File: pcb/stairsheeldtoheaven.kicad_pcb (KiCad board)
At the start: 2 copper layers, 105.4 x 97.8 mm, 27 parts, among them P1 CONN_10X2, P10 5, P11 6, P12 7, P13 8, P14 9, P15 10, P16 11, P17 12, P18 13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

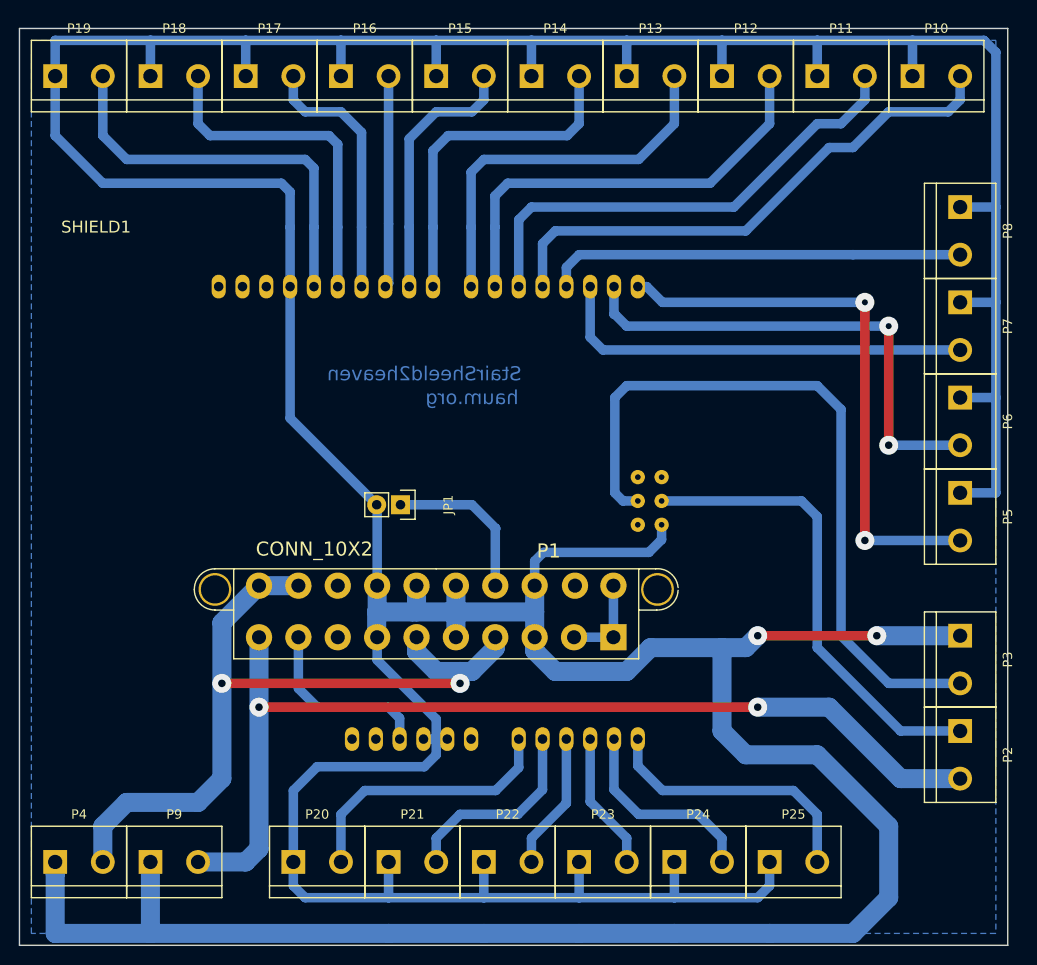
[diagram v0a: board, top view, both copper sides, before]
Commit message: simplification connection LED
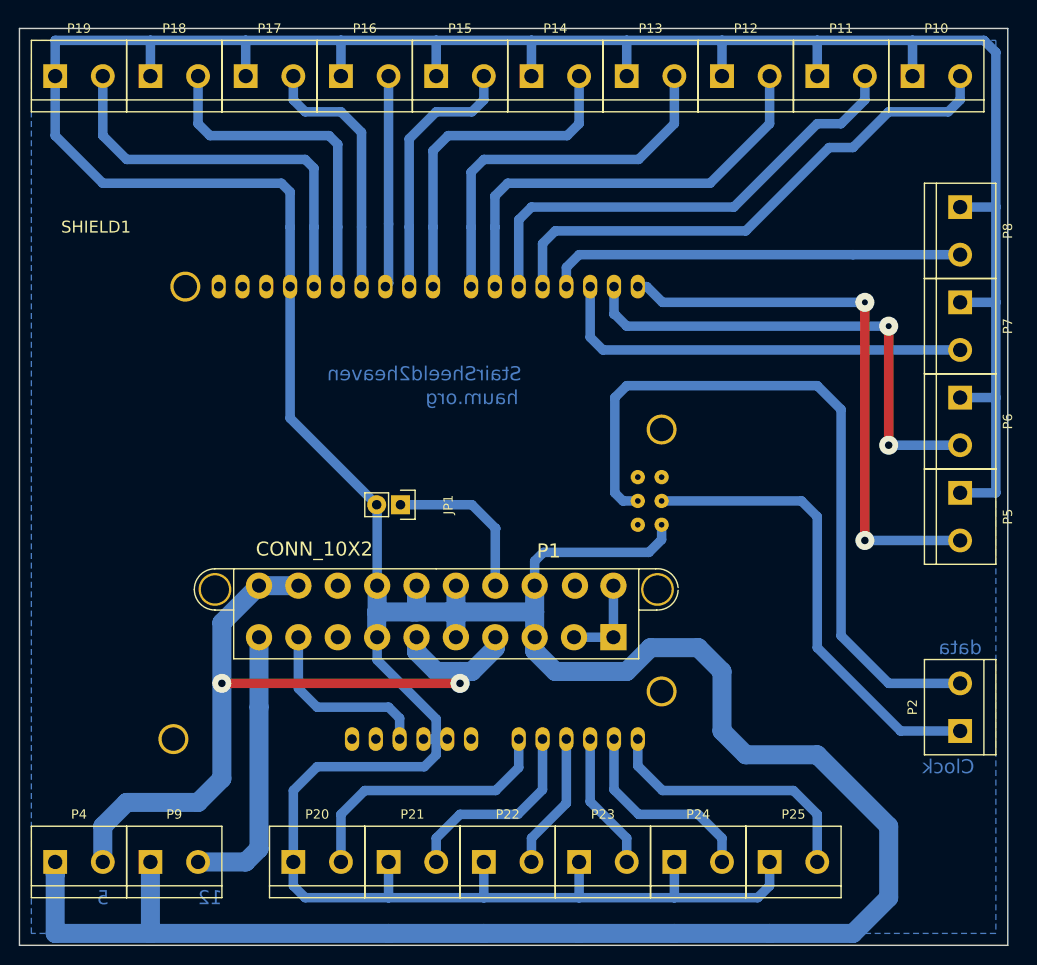
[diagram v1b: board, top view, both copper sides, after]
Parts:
- removed P3: LED2, Connect:bornier2
- SHIELD1: footprint JbLb_lib:ARDUINO_SHIELD_R3 -> haum_libs:ARDUINO_SHIELD_R3
- moved P2 5.08 mm to (175.3, 91.4), turned to 90 degrees
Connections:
- P2 pad 2: /12V -> /clock
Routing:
- net /12V: track 107.6 -> 29.6 mm, vias 2 -> 0
- net GND: track 645.0 -> 617.6 mm, vias 2 -> 0
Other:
- board text added: "12"
- board text added: "5"
- board text added: "Clock"
- board text added: "data"

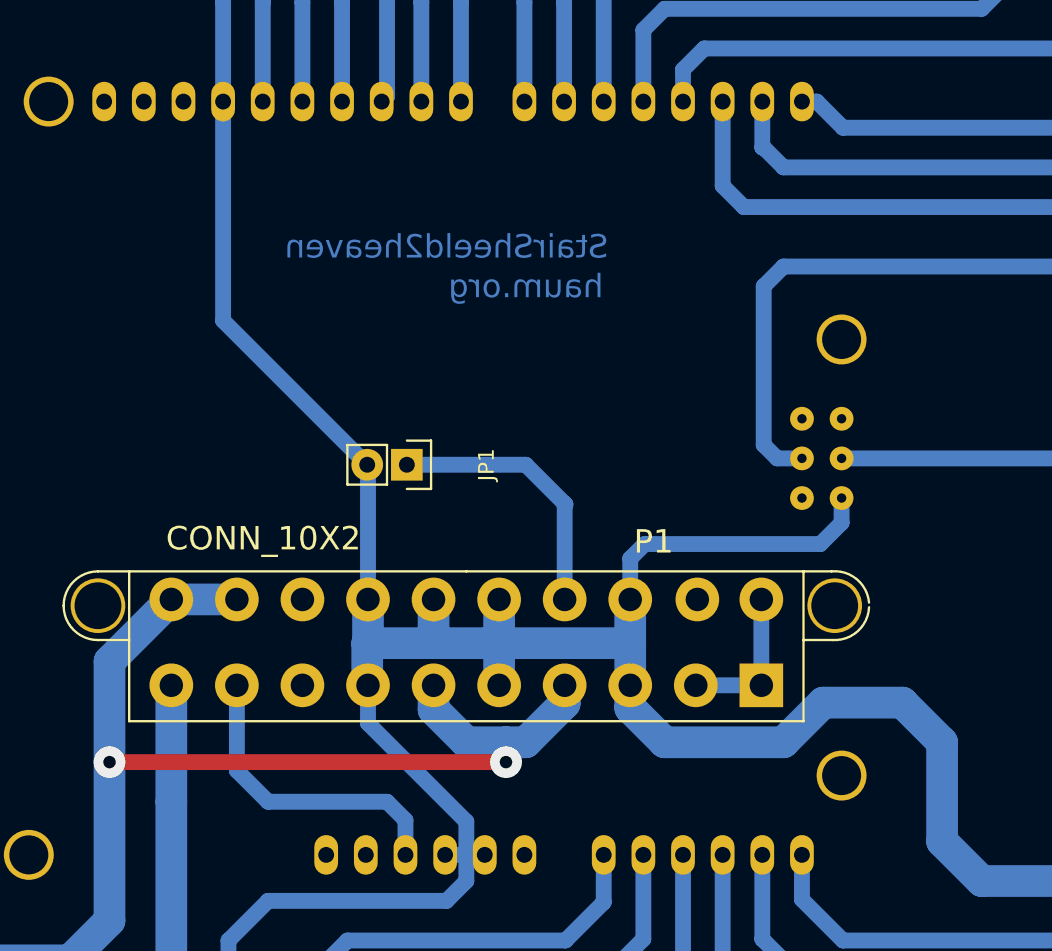
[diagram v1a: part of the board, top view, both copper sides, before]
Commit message: Ajout pin PowerGood redefinition plan de masse regénération fichiers de fabrication
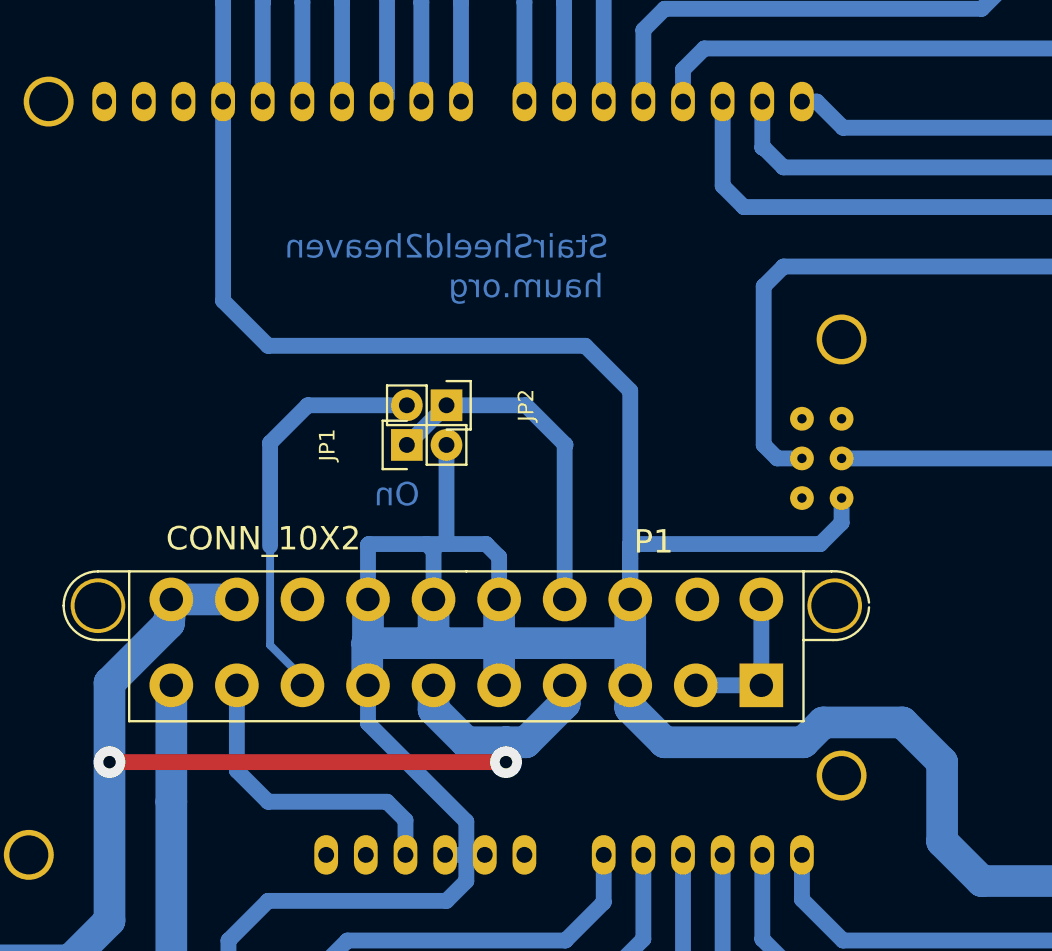
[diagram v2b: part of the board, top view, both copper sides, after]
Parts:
- added JP2: JUMPER, Pin_Headers:Pin_Header_Straight_1x02, F.Cu at (118.1, 66.0)
- moved JP1 1.27 mm to (115.6, 68.6), turned to 90 degrees
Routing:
- net GND: track 617.6 -> 660.3 mm
- net /PG: track 0.00 -> 26.1 mm
- net /PSON: track 17.4 -> 22.2 mm
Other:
- net class piste_cmdS added: clearance 0.254, trace_width 0.6, via_dia 0.889, via_drill 0.635
- board text added: "On"
